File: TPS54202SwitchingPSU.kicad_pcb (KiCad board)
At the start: 2 copper layers, 10 parts, among them CN1 Header_2_pin, CN2 Header_2_pin, U2 TPS54202DDC

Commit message: Rev A production release
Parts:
- moved C1 47.9 mm to (122.9, 85.9), turned to 180 degrees
- moved L1 40.1 mm to (134.4, 89.1), turned to 90 degrees
- moved C2 29.7 mm to (139.7, 89.1), turned to -90 degrees
- moved CN2 9.57 mm to (143.8, 87.5)
- moved CN1 1.27 mm to (115.2, 87.5)
- moved U2 1.11 mm to (122.9, 90.2)
- moved R11 1.01 mm to (128.3, 87.0)
- moved C12 0.91 mm to (128.5, 92.0)
- moved R12 0.89 mm to (128.3, 89.8)
- moved C3 0.81 mm to (119.1, 88.9)
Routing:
- net Net-(U2-SW): track 0.00 -> 17.6 mm, vias 0 -> 6
- net /Vout: track 0.00 -> 16.1 mm
- net /Vin: track 0.00 -> 9.06 mm
- net Net-(U2-FB): track 0.00 -> 8.94 mm
- net GND: track 0.00 -> 7.76 mm, vias 0 -> 6
- net Net-(U2-BOOT): track 0.00 -> 3.49 mm
- net unconnected-(U2-EN-Pad5): track 0.00 -> 2.88 mm, vias 0 -> 1
- added copper zone on F.Cu, net /Vin
- added copper zone on F.Cu, net /Vout
- added copper zone on B.Cu, net GND
- added copper zone on F.Cu, net GND
- added copper zone on B.Cu, net Net-(U2-SW)
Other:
- board outline added: 35 x 11 mm
- board text added: "+"
- board text added: "-"
- board text added: "AD Gaming"
- board text added: "IN"
- board text added: "OUT"
- board text added: "Rev A"
- board text added: "TPS54202 PSU"

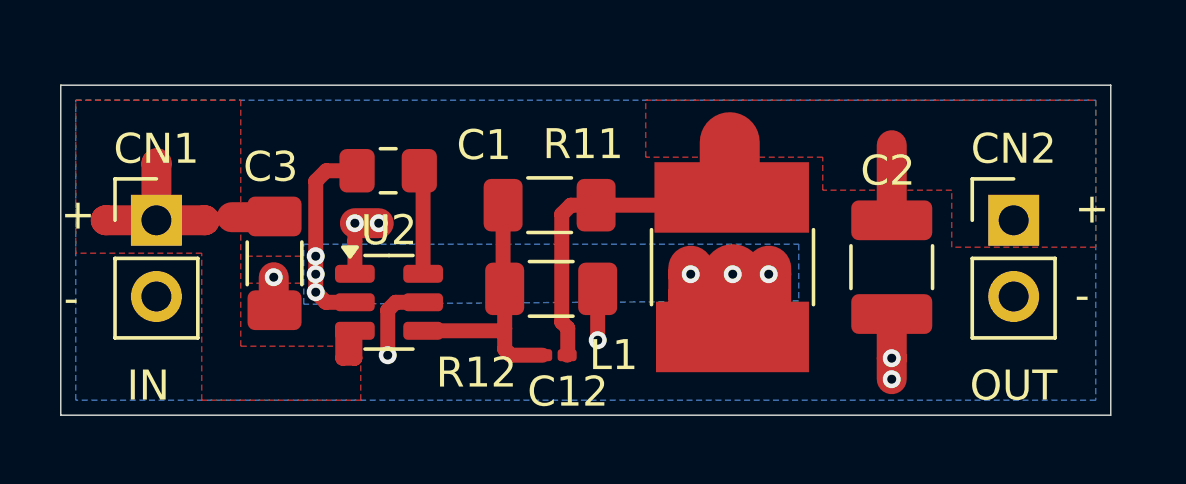
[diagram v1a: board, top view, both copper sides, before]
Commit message: Updated to Rev B to fix board errors
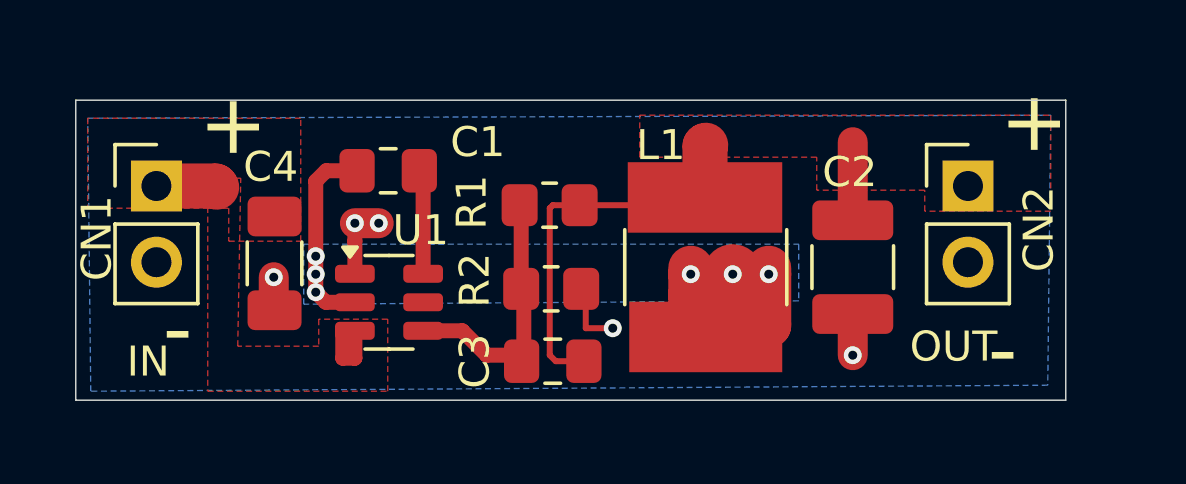
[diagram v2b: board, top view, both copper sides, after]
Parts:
- C3: renamed from C12; value 68pF 25V -> 68pF; footprint Capacitor_SMD:C_0201_0603Metric_Pad0.64x0.40mm_HandSolder -> Capacitor_SMD:C_0805_2012Metric_Pad1.18x1.45mm_HandSolder
- R1: renamed from R11; footprint Resistor_SMD:R_1206_3216Metric_Pad1.30x1.75mm_HandSolder -> Resistor_SMD:R_0805_2012Metric_Pad1.20x1.40mm_HandSolder
- R2: renamed from R12; footprint Resistor_SMD:R_1206_3216Metric_Pad1.30x1.75mm_HandSolder -> Resistor_SMD:R_0805_2012Metric_Pad1.20x1.40mm_HandSolder
- moved CN2 1.91 mm to (142.2, 86.4)
- moved C2 1.30 mm to (138.4, 89.1)
- moved CN1 1.14 mm to (115.2, 86.4)
- moved L1 0.89 mm to (133.5, 89.1)
- moved C3 0.21 mm to (128.4, 92.2)
- renumbered C3 to C4, U2 to U1
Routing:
- net /Vin: track 9.06 -> 4.30 mm
- net unconnected-(U1-EN-Pad5): track 2.88 -> 0.09 mm, vias 1 -> 0
- net /Vout: track 16.1 -> 18.6 mm
- net GND: track 7.76 -> 7.52 mm, vias 6 -> 5
- removed copper zone on F.Cu, net GND
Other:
- board size 35 x 11 mm -> 33 x 10 mm
- board text added: "Rev B"
- board text removed: "Rev A"
